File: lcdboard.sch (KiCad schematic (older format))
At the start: 68 parts, among them J1 Conn_02x05_Odd_Even, J2 Conn_02x25_Counter_Clockwise, J3 Conn_02x12_Counter_Clockwise, J4 USB_B_Micro, J5 Conn_01x03, SW1 SW_Push, SW3 SW_SPST, U1 MK82FN256VLL15, U2 Serial-Flash, U3 TPS61169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

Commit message: Connect backlight supply to VREGIN
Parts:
- C15: MFR Kemet -> Walsin; MPN C1206C475K4NACAUTO -> 0805B475K6R3CT
- SW1: MFR E-Switch -> C&K; MPN TL3302AF180QG -> KSR251GLFS
- SW3: MPN PCM13SMTR -> PCM12SMTR
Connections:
- wire segments 264 -> 265
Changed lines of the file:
@@
 EESchema Schematic File Version 4
 LIBS:camboard-cache
-EELAYER 26 0
+EELAYER 29 0
 EELAYER END
 $Descr A4 11693 8268
@@
 F 2 "Switches:TACTILE_SWITCH_SMD_6.0X3.5MM" H 2000 7450 50  0001 C CNN
 F 3 "" H 2000 7450 50  0001 C CNN
-F 4 "E-Switch" H 0   0   50  0001 C CNN "MFR"
-F 5 "TL3302AF180QG" H 0   0   50  0001 C CNN "MPN"
+F 4 "C&K" H 0   0   50  0001 C CNN "MFR"
+F 5 "KSR251GLFS" H 0   0   50  0001 C CNN "MPN"
 	1    2000 7250
 	0    1    1    0
@@
 Wire Wire Line
 	7450 950  7250 950
-$Comp
-L power:+3.3V #PWR0135
-U 1 1 5C79CEEB
-P 6900 950
-F 0 "#PWR0135" H 6900 800 50  0001 C CNN
-F 1 "+3.3V" H 6915 1123 50  0000 C CNN
-F 2 "" H 6900 950 50  0001 C CNN
-F 3 "" H 6900 950 50  0001 C CNN
-	1    6900 950
-	1    0    0    -1
-$EndComp
 Connection ~ 7250 950
 $Comp
@@
 F 2 "Capacitor_SMD:C_0805_2012Metric" H 6900 1050 50  0001 C CNN
 F 3 "~" H 6900 1050 50  0001 C CNN
-F 4 "Kemet" H 0   0   50  0001 C CNN "MFR"
-F 5 "C1206C475K4NACAUTO" H 0   0   50  0001 C CNN "MPN"
+F 4 "Walsin" H 0   0   50  0001 C CNN "MFR"
+F 5 "0805B475K6R3CT" H 0   0   50  0001 C CNN "MPN"
 	1    6900 1050
 	1    0    0    -1
@@
 $EndComp
 Wire Wire Line
-	6900 950  7250 950
-Connection ~ 6900 950
+	6600 950  6900 950
 $Comp
 L Device:C_Small C16
@@
 F 3 "" H 7050 4750 50  0001 C CNN
 F 4 "C&K" H 7050 4750 50  0001 C CNN "MFR"
-F 5 "PCM13SMTR" H 7050 4750 50  0001 C CNN "MPN"
+F 5 "PCM12SMTR" H 7050 4750 50  0001 C CNN "MPN"
 	1    7050 4750
 	1    0    0    -1
@@
 $EndComp
 NoConn ~ 1300 4800
+Connection ~ 6900 950
+Wire Wire Line
+	6900 950  7250 950
+Text Label 6600 950  0    50   ~ 0
+VDD_REGIN
 $EndSCHEMATC

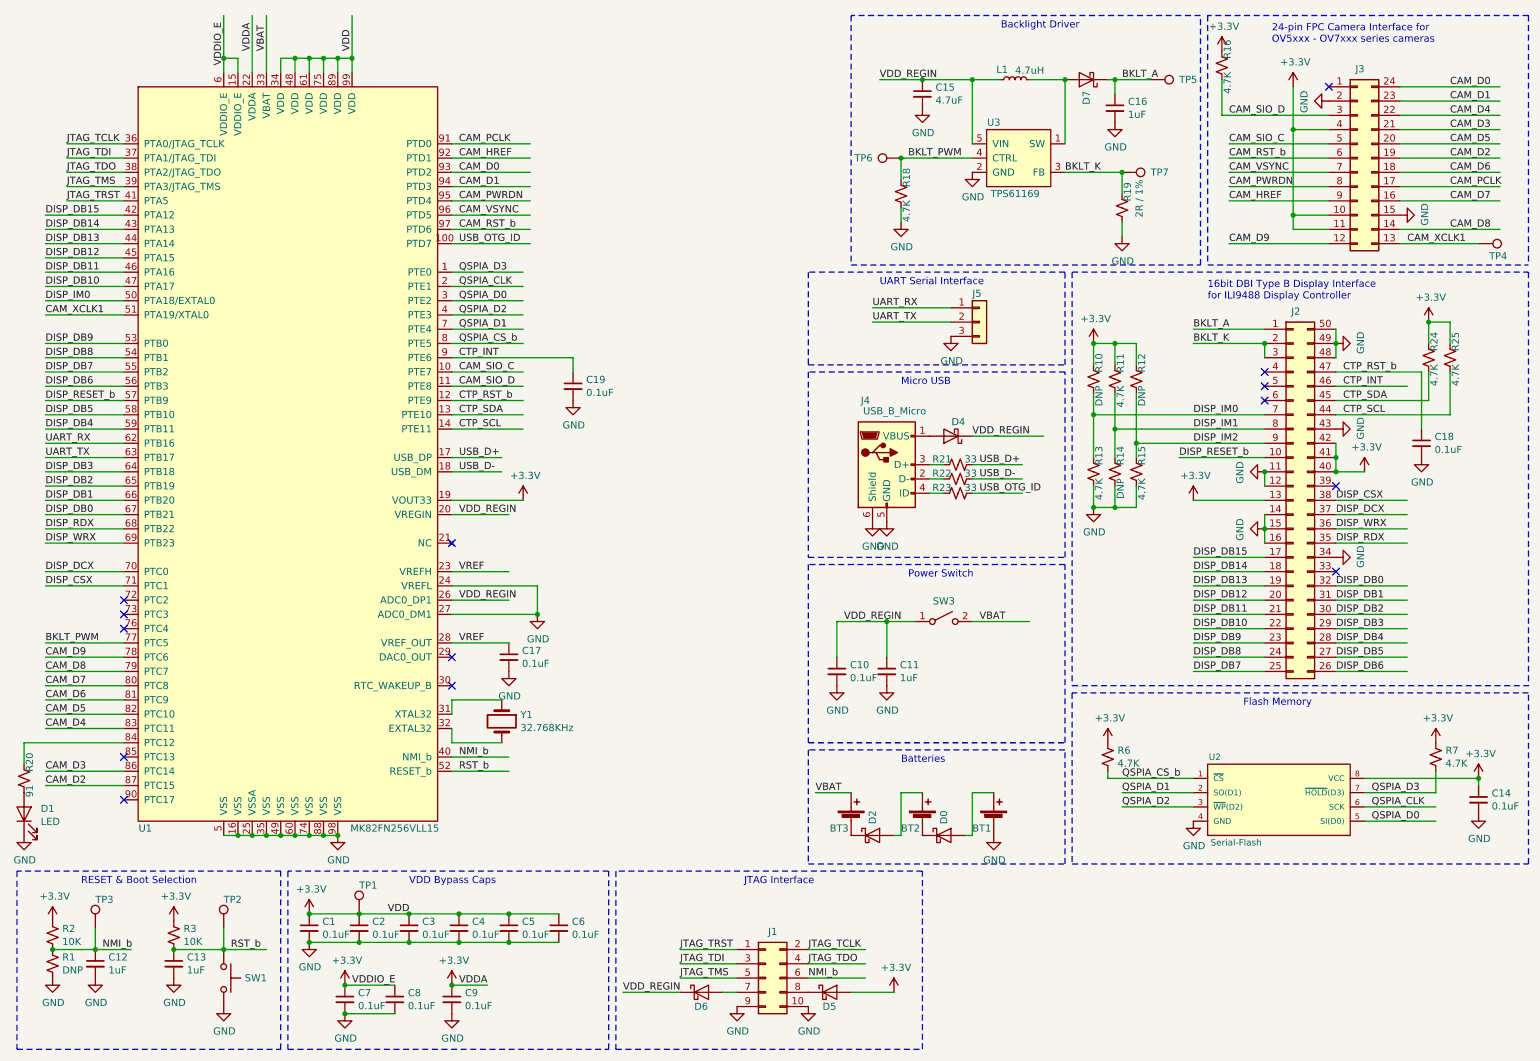
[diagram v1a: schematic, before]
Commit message: Add external oscillator
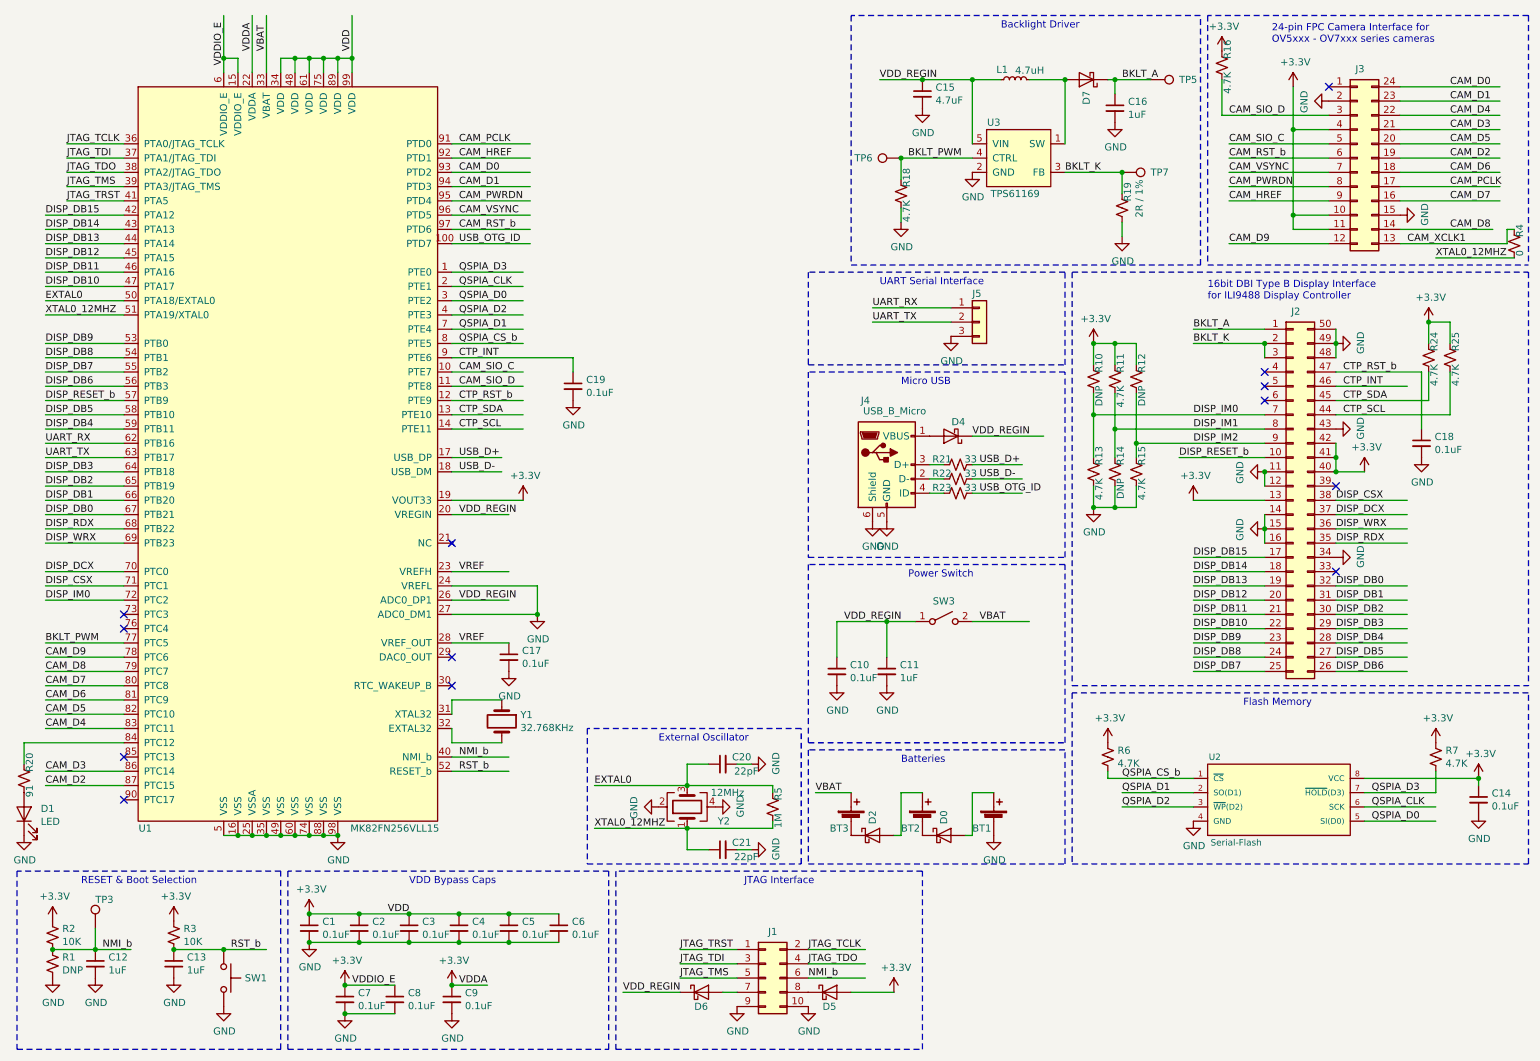
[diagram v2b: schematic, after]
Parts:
- removed TP1, TP2, TP4: TestPoint, TestPoint:TestPoint_Pad_D1.5mm, symbol Connector:TestPoint
- added C20, C21: 22pF, Capacitor_SMD:C_0402_1005Metric, symbol Device:C_Small
- added R4: 0, Resistor_SMD:R_0402_1005Metric, symbol Device:R_Small_US
- added R5: 1M, Resistor_SMD:R_0402_1005Metric, symbol Device:R_Small_US
- added Y2: 12MHz, Oscillator:Oscillator_SMD_EuroQuartz_XO53-4Pin_5.0x3.2mm_HandSoldering, symbol Device:Crystal_GND24
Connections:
- net labels added: EXTAL0, XTAL0_12MHZ
- wire segments 265 -> 280
- no-connect marks 14 -> 13
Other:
- note added: "External Oscillator"
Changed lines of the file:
@@
 EESchema Schematic File Version 4
-LIBS:camboard-cache
-EELAYER 29 0
+EELAYER 30 0
 EELAYER END
 $Descr A4 11693 8268
@@
 Text Notes 1000 6600 0    50   ~ 0
 RESET & Boot Selection
-Wire Wire Line
-	2000 7050 2000 6900
 Wire Wire Line
 	1100 7050 1100 6900
@@
 Text Label 750  3000 0    50   ~ 0
 DISP_DB7
-Text Label 750  2500 0    50   ~ 0
+Text Label 750  4600 0    50   ~ 0
 DISP_IM0
-Text Label 750  2600 0    50   ~ 0
-CAM_XCLK1
 Wire Wire Line
 	750  1900 1300 1900
@@
 CAM_D8
 Wire Wire Line
-	10250 2000 10950 2000
+	10250 2000 10900 2000
 Text Label 10600 1800 0    50   ~ 0
 CAM_D7
@@
 	750  2400 1300 2400
 Wire Wire Line
-	750  2500 1300 2500
-Wire Wire Line
-	750  2600 1300 2600
+	750  4600 1300 4600
 Wire Wire Line
 	750  2800 1300 2800
@@
 Wire Wire Line
 	9000 950  9000 1200
-Wire Wire Line
-	10250 2100 10800 2100
 Text Label 10300 2100 0    50   ~ 0
 CAM_XCLK1
-$Comp
-L Connector:TestPoint TP4
-U 1 1 5CEA5D62
-P 10800 2100
-F 0 "TP4" V 10858 2174 50  0000 L TNN
-F 1 "TestPoint" H 10858 2129 50  0001 L CNN
-F 2 "TestPoint:TestPoint_Pad_D1.5mm" H 11000 2100 50  0001 C CNN
-F 3 "~" H 11000 2100 50  0001 C CNN
-	1    10800 2100
-	0    1    1    0
-$EndComp
 Wire Wire Line
 	750  5000 1300 5000
@@
 Wire Notes Line
 	6100 4350 6100 5600
-NoConn ~ 1300 4600
-NoConn ~ 1300 4700
 NoConn ~ 3600 5000
 NoConn ~ 3600 5200
-NoConn ~ 1300 6000
 NoConn ~ 1300 5700
 $Comp
@@
 	6400 7350 6700 7350
 $Comp
-L Connector:TestPoint TP1
-U 1 1 5C9A3DFD
-P 2950 6800
-F 0 "TP1" H 2950 7000 50  0000 L CNN
-F 1 "TestPoint" H 3008 6829 50  0001 L CNN
-F 2 "TestPoint:TestPoint_Pad_D1.5mm" H 3150 6800 50  0001 C CNN
-F 3 "~" H 3150 6800 50  0001 C CNN
-	1    2950 6800
-	1    0    0    -1
-$EndComp
-$Comp
-L Connector:TestPoint TP2
-U 1 1 5CB03011
-P 2000 6900
-F 0 "TP2" H 2000 7100 50  0000 L CNN
-F 1 "TestPoint" H 2058 6929 50  0001 L CNN
-F 2 "TestPoint:TestPoint_Pad_D1.5mm" H 2200 6900 50  0001 C CNN
-F 3 "~" H 2200 6900 50  0001 C CNN
-	1    2000 6900
-	1    0    0    -1
-$EndComp
-$Comp
 L Connector:TestPoint TP3
 U 1 1 5CB350AA
@@
 Text Label 6600 950  0    50   ~ 0
 VDD_REGIN
+Text Label 750  2600 0    50   ~ 0
+XTAL0_12MHZ
+Wire Wire Line
+	750  2600 1300 2600
+Text Label 750  2500 0    50   ~ 0
+EXTAL0
+Wire Wire Line
+	750  2500 1300 2500
+Text Label 4600 6200 0    50   ~ 0
+XTAL0_12MHZ
+Wire Wire Line
+	4600 6200 5250 6200
+Text Label 4600 5900 0    50   ~ 0
+EXTAL0
+NoConn ~ 1300 6000
+NoConn ~ 1300 4700
+Wire Wire Line
+	10500 2200 11050 2200
+Text Label 10500 2200 0    50   ~ 0
+XTAL0_12MHZ
+$Comp
+L Device:R_Small_US R4
+U 1 1 5DC690B7
+P 11050 2100
+F 0 "R4" V 11118 2146 50  0000 L BNN
+F 1 "0" V 11118 2055 50  0000 R BNN
+F 2 "Resistor_SMD:R_0402_1005Metric" H 11050 2100 50  0001 C CNN
+F 3 "~" H 11050 2100 50  0001 C CNN
+F 4 "Vishay" H 450 -800 50  0001 C CNN "MFR"
+F 5 "CRCW04024K70JNEDC" H 450 -800 50  0001 C CNN "MPN"
+	1    11050 2100
+	1    0    0    -1
+$EndComp
+Wire Wire Line
+	11000 2100 11000 2000
+Wire Wire Line
+	11000 2000 11050 2000
+Wire Wire Line
+	10250 2100 11000 2100
+$Comp
+L Device:Crystal_GND24 Y2
+U 1 1 5DD5DD61
+P 5250 6050
+F 0 "Y2" V 5150 5750 50  0000 L CNN
+F 1 "12MHz" V 5350 5650 50  0000 L CNN
+F 2 "Oscillator:Oscillator_SMD_EuroQuartz_XO53-4Pin_5.0x3.2mm_HandSoldering" H 5250 6050 50  0001 C CNN
+F 3 "~" H 5250 6050 50  0001 C CNN
+F 4 "Pletronics Inc." H 1300 600 50  0001 C CNN "MFR"
+F 5 "SM11T-22-12.0M-30H1CG" H 1300 600 50  0001 C CNN "MPN"
+	1    5250 6050
+	0    -1   -1   0
+$EndComp
+$Comp
+L Device:R_Small_US R5
+U 1 1 5DDFC134
+P 5850 6050
+F 0 "R5" V 5918 6096 50  0000 L BNN
+F 1 "1M" V 5918 6005 50  0000 R BNN
+F 2 "Resistor_SMD:R_0402_1005Metric" H 5850 6050 50  0001 C CNN
+F 3 "~" H 5850 6050 50  0001 C CNN
+F 4 "Vishay" H -4750 3150 50  0001 C CNN "MFR"
+F 5 "CRCW04024K70JNEDC" H -4750 3150 50  0001 C CNN "MPN"
+	1    5850 6050
+	1    0    0    -1
+$EndComp
+Wire Wire Line
+	5850 5950 5850 5900
+Wire Wire Line
+	5850 5900 5250 5900
+Wire Wire Line
+	5850 6150 5850 6200
+$Comp
+L Device:C_Small C21
+U 1 1 5DE687B0
+P 5500 6350
+F 0 "C21" V 5550 6150 50  0000 L CNN
+F 1 "22pF" V 5450 6100 50  0000 L CNN
+F 2 "Capacitor_SMD:C_0402_1005Metric" H 5500 6350 50  0001 C CNN
+F 3 "~" H 5500 6350 50  0001 C CNN
+F 4 "Kemet" H -800 1250 50  0001 C CNN "MFR"
+F 5 "C0402C104K4RAC7411" H -800 1250 50  0001 C CNN "MPN"
+	1    5500 6350
+	0    -1   -1   0
+$EndComp
+$Comp
+L power:GND #PWR02
+U 1 1 5DE687BA
+P 5700 6350
+F 0 "#PWR02" H 5700 6100 50  0001 C CNN
+F 1 "GND" H 5705 6177 50  0000 C CNN
+F 2 "" H 5700 6350 50  0001 C CNN
+F 3 "" H 5700 6350 50  0001 C CNN
+	1    5700 6350
+	0    -1   -1   0
+$EndComp
+Wire Wire Line
+	5600 6350 5700 6350
+$Comp
+L Device:C_Small C20
+U 1 1 5DF7E070
+P 5500 5750
+F 0 "C20" V 5550 5550 50  0000 L CNN
+F 1 "22pF" V 5450 5500 50  0000 L CNN
+F 2 "Capacitor_SMD:C_0402_1005Metric" H 5500 5750 50  0001 C CNN
+F 3 "~" H 5500 5750 50  0001 C CNN
+F 4 "Kemet" H -800 650 50  0001 C CNN "MFR"
+F 5 "C0402C104K4RAC7411" H -800 650 50  0001 C CNN "MPN"
+	1    5500 5750
+	0    -1   -1   0
+$EndComp
+$Comp
+L power:GND #PWR01
+U 1 1 5DF7E07A
+P 5700 5750
+F 0 "#PWR01" H 5700 5500 50  0001 C CNN
+F 1 "GND" H 5705 5577 50  0000 C CNN
+F 2 "" H 5700 5750 50  0001 C CNN
+F 3 "" H 5700 5750 50  0001 C CNN
+	1    5700 5750
+	0    -1   -1   0
+$EndComp
+Wire Wire Line
+	5600 5750 5700 5750
+Wire Notes Line
+	6050 6450 6050 5500
+Wire Notes Line
+	6050 5500 4550 5500
+Wire Notes Line
+	4550 5500 4550 6450
+Wire Notes Line
+	4550 6450 6050 6450
+Text Notes 5050 5600 0    50   ~ 0
+External Oscillator
+Wire Wire Line
+	4600 5900 5250 5900
+Wire Wire Line
+	5850 6200 5250 6200
+Connection ~ 5250 5900
+Connection ~ 5250 6200
+Wire Wire Line
+	5400 6350 5250 6350
+Wire Wire Line
+	5250 5750 5400 5750
+$Comp
+L power:GND #PWR0135
+U 1 1 5E362CDB
+P 5450 6050
+F 0 "#PWR0135" H 5450 5800 50  0001 C CNN
+F 1 "GND" H 5455 5877 50  0000 C CNN
+F 2 "" H 5450 6050 50  0001 C CNN
+F 3 "" H 5450 6050 50  0001 C CNN
+	1    5450 6050
+	0    -1   -1   0
+$EndComp
+$Comp
+L power:GND #PWR0141
+U 1 1 5E3850B0
+P 5050 6050
+F 0 "#PWR0141" H 5050 5800 50  0001 C CNN
+F 1 "GND" H 5055 5877 50  0000 C CNN
+F 2 "" H 5050 6050 50  0001 C CNN
+F 3 "" H 5050 6050 50  0001 C CNN
+	1    5050 6050
+	0    1    1    0
+$EndComp
+Wire Wire Line
+	5250 6200 5250 6350
+Wire Wire Line
+	5250 5750 5250 5900
 $EndSCHEMATC

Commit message: Add pull-up to JTAG_TRST and remove from header
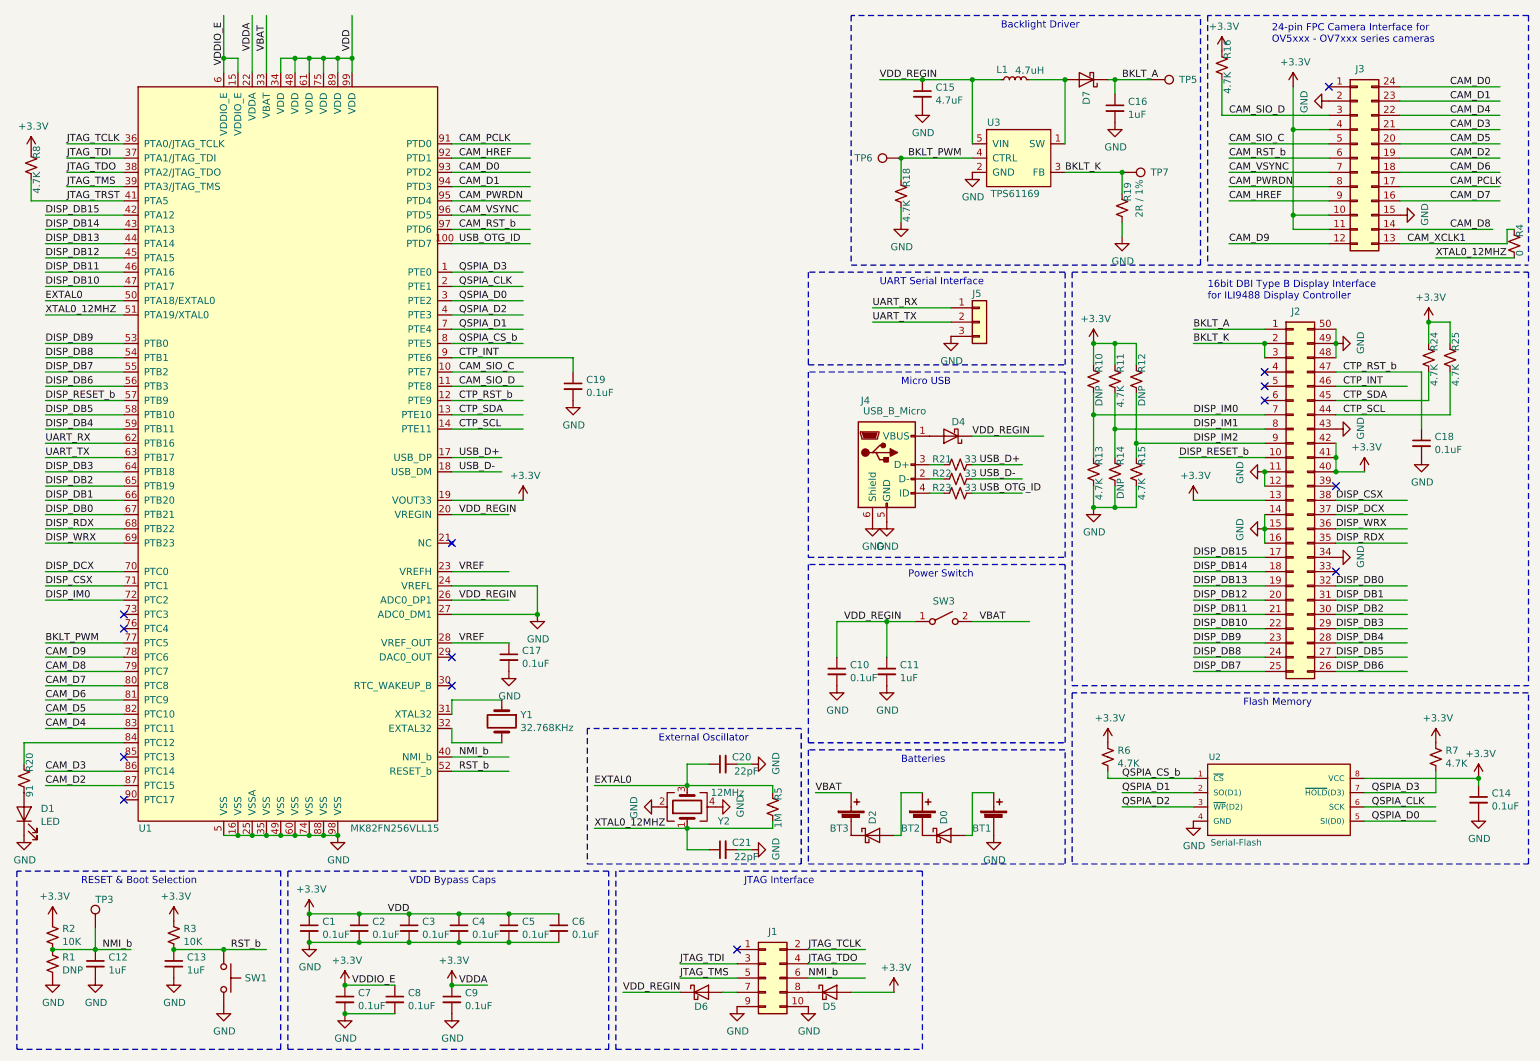
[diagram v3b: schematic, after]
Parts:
- added R8: 4.7K, Resistor_SMD:R_0402_1005Metric, symbol Device:R_Small_US
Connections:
- no-connect marks 13 -> 14
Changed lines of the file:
@@
 EESchema Schematic File Version 4
+LIBS:smirk-pcb-cache
 EELAYER 30 0
 EELAYER END
@@
 JTAG Interface
 Wire Wire Line
-	5200 7050 5600 7050
-Wire Wire Line
 	5200 7150 5600 7150
 Wire Wire Line
@@
 	1    0    0    -1
 $EndComp
-Text Label 5200 7050 0    50   ~ 0
-JTAG_TRST
 Text Label 6100 7050 0    50   ~ 0
 JTAG_TCLK
@@
 Wire Notes Line
 	4750 7750 6900 7750
-Wire Wire Line
-	900  1800 1300 1800
 Wire Wire Line
 	900  1500 1300 1500
@@
 Wire Wire Line
 	5250 5750 5250 5900
+$Comp
+L Device:R_Small_US R8
+U 1 1 5D8CBE3A
+P 650 1550
+F 0 "R8" V 718 1596 50  0000 L BNN
+F 1 "4.7K" V 718 1505 50  0000 R BNN
+F 2 "Resistor_SMD:R_0402_1005Metric" H 650 1550 50  0001 C CNN
+F 3 "~" H 650 1550 50  0001 C CNN
+F 4 "Vishay" H -7750 -2150 50  0001 C CNN "MFR"
+F 5 "CRCW04024K70JNEDC" H -7750 -2150 50  0001 C CNN "MPN"
+	1    650  1550
+	1    0    0    -1
+$EndComp
+$Comp
+L power:+3.3V #PWR03
+U 1 1 5D946CF3
+P 650 1450
+F 0 "#PWR03" H 650 1300 50  0001 C CNN
+F 1 "+3.3V" H 665 1623 50  0000 C CNN
+F 2 "" H 650 1450 50  0001 C CNN
+F 3 "" H 650 1450 50  0001 C CNN
+	1    650  1450
+	1    0    0    -1
+$EndComp
+Wire Wire Line
+	650  1800 650  1650
+Wire Wire Line
+	650  1800 1300 1800
+NoConn ~ 5600 7050
 $EndSCHEMATC
